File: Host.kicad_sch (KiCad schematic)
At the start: 15 parts, among them J2 UJ2-MBH-1-SMT-TR, U2 MPM3612-33, U3 STM32G061GxUx

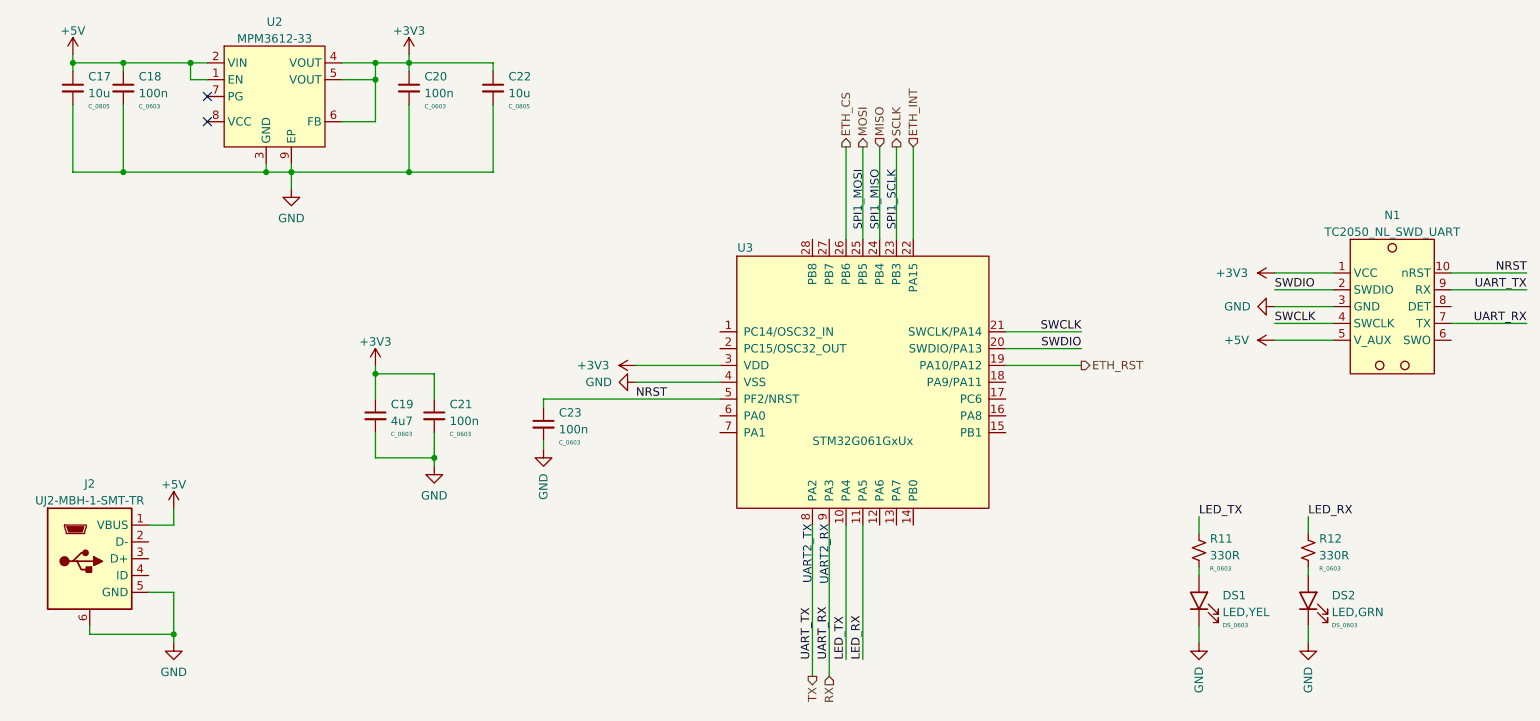
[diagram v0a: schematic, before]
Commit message: Rebuild using new output scripts
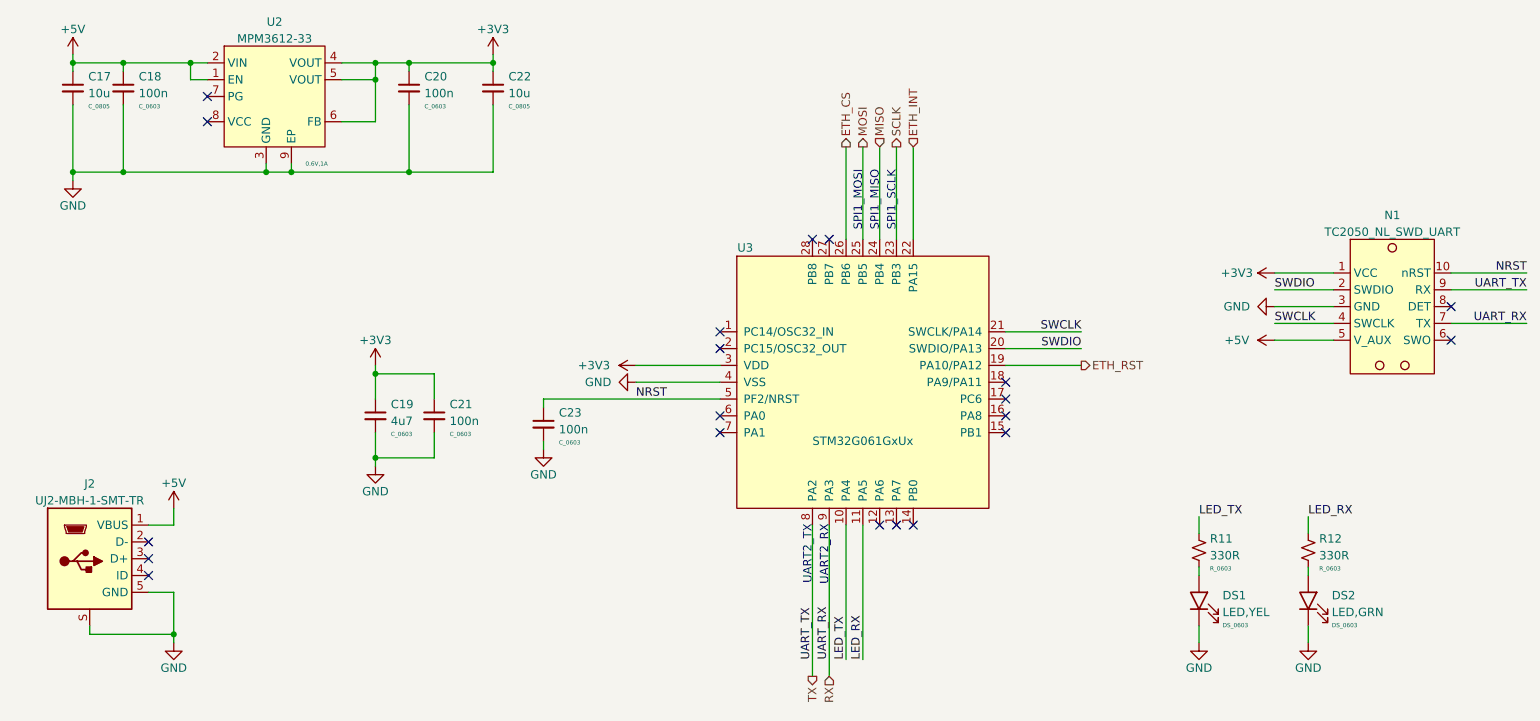
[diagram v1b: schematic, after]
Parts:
- U2: Params (none) -> 0.6V,1A
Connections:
- net GND: now also J2.S; no longer J2.6
- no-connect marks 2 -> 20
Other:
- company: (none) -> TL Embedded Ltd
- title: (none) -> Serial-Ethernet
